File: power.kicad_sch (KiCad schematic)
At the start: 25 parts, among them IC4 BQ27441DRZR-G1A, IC5 MCP73811T-420I_OT, IC6 TPS62237DRYR, IC7 ST1S15J18R, U1 TPS62233DRYR

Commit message: Add company name (using github URL), date, and change revision number to all schematic pages
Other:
- company: (none) -> github.com/fuad1502/open-running-watch-hw
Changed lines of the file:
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@@
 	(title_block
 		(title "Open Running Watch")
-		(rev "A")
+		(date "2024-04-12")
+		(rev "0.1.0")
+		(company "github.com/fuad1502/open-running-watch-hw")
 	)
 	(junction

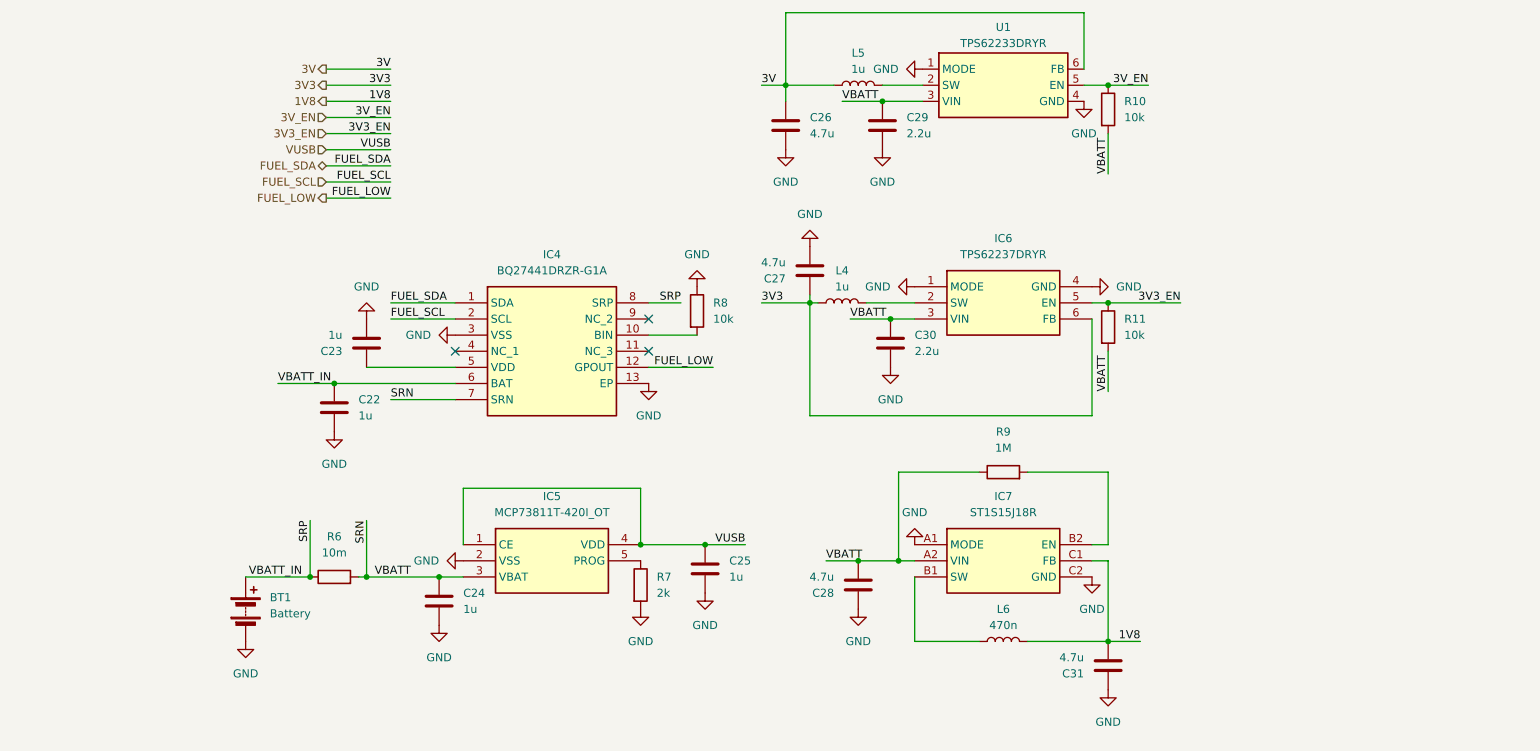
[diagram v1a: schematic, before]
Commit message: Add 5V boost switching regulator
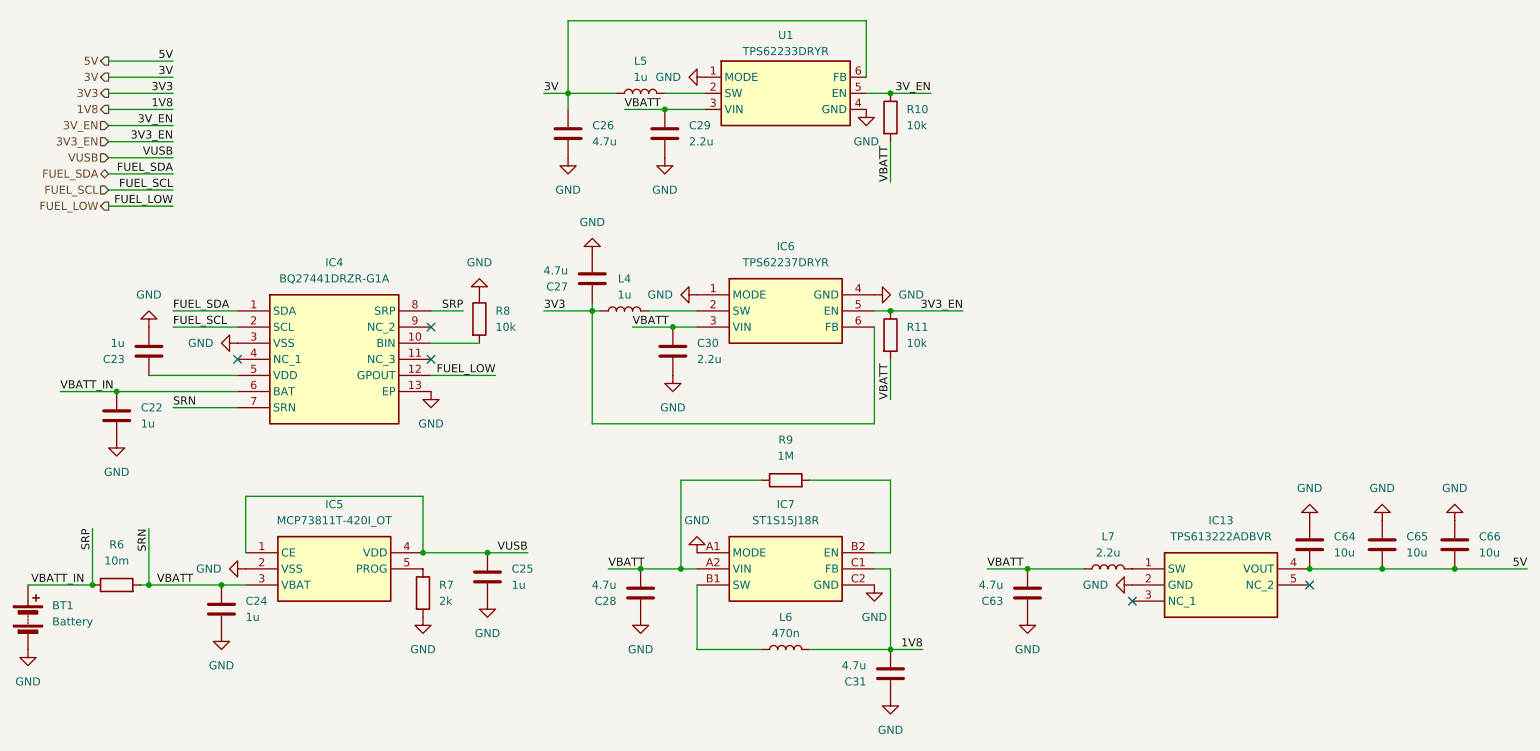
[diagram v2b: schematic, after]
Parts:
- added C63: 4.7u, Capacitor_SMD:C_0402_1005Metric_Pad0.74x0.62mm_HandSolder, symbol Device:C
- added C64, C65, C66: 10u, Capacitor_SMD:C_0603_1608Metric, symbol Device:C
- added IC13: TPS613222ADBVR, SOT95P280X145-5N, symbol TPS613222ADBVR:TPS613222ADBVR
- added L7: 2.2u, Inductor_SMD:L_1008_2520Metric, symbol Device:L
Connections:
- net GND: now also C63.1, C64.1, C65.1, C66.1, IC13.2 (GND)
- net SRN: now also C63.2, L7.1
- new net: IC13.1 (SW), L7.2
- new net 5V: C64.2, C65.2, C66.2, IC13.4 (VOUT)
- no-connect marks 3 -> 5
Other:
- moved on the sheet: BT1, C22, C23, C24, C25, C26, C27, C28, C29, C30, C31, IC4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

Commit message: Changed to smaller tactile switch
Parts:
- IC13: footprint SOT95P280X145-5N -> TPS613222ADBVR:SOT95P280X145-5N
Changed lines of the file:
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@@
 			)
 		)
-		(property "Footprint" "SOT95P280X145-5N"
+		(property "Footprint" "TPS613222ADBVR:SOT95P280X145-5N"
 			(at 233.68 221.92 0)
 			(effects

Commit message: Changed hand soldered footprints to normal footprints
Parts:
- C22, C23, C24, C25: footprint Capacitor_SMD:C_0603_1608Metric_Pad1.08x0.95mm_HandSolder -> Capacitor_SMD:C_0603_1608Metric
- C26, C27, C28, C29, C30, C31, C63: footprint Capacitor_SMD:C_0402_1005Metric_Pad0.74x0.62mm_HandSolder -> Capacitor_SMD:C_0402_1005Metric
- L4, L5: footprint Inductor_SMD:L_1008_2520Metric_Pad1.43x2.20mm_HandSolder -> Inductor_SMD:L_1008_2520Metric
- L6: footprint Inductor_SMD:L_0805_2012Metric_Pad1.05x1.20mm_HandSolder -> Inductor_SMD:L_0805_2012Metric
- R10, R11, R7, R8, R9: footprint Resistor_SMD:R_0402_1005Metric_Pad0.72x0.64mm_HandSolder -> Resistor_SMD:R_0402_1005Metric
- R6: footprint Resistor_SMD:R_1206_3216Metric_Pad1.30x1.75mm_HandSolder -> Resistor_SMD:R_1206_3216Metric
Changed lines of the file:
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@@
 			)
 		)
-		(property "Footprint" "Resistor_SMD:R_0402_1005Metric_Pad0.72x0.64mm_HandSolder"
+		(property "Footprint" "Resistor_SMD:R_0402_1005Metric"
 			(at 169.672 55.88 90)
 			(effects
@@
 			)
 		)
-		(property "Footprint" "Resistor_SMD:R_0402_1005Metric_Pad0.72x0.64mm_HandSolder"
+		(property "Footprint" "Resistor_SMD:R_0402_1005Metric"
 			(at 154.94 114.808 90)
 			(effects
@@
 			)
 		)
-		(property "Footprint" "Inductor_SMD:L_1008_2520Metric_Pad1.43x2.20mm_HandSolder"
+		(property "Footprint" "Inductor_SMD:L_1008_2520Metric"
 			(at 129.54 86.36 0)
 			(effects
@@
 			)
 		)
-		(property "Footprint" "Capacitor_SMD:C_0603_1608Metric_Pad1.08x0.95mm_HandSolder"
+		(property "Footprint" "Capacitor_SMD:C_0603_1608Metric"
 			(at 53.6448 88.9 0)
 			(effects
@@
 			)
 		)
-		(property "Footprint" "Capacitor_SMD:C_0603_1608Metric_Pad1.08x0.95mm_HandSolder"
+		(property "Footprint" "Capacitor_SMD:C_0603_1608Metric"
 			(at 108.9152 132.08 0)
 			(effects
@@
 			)
 		)
-		(property "Footprint" "Capacitor_SMD:C_0603_1608Metric_Pad1.08x0.95mm_HandSolder"
+		(property "Footprint" "Capacitor_SMD:C_0603_1608Metric"
 			(at 50.4952 106.68 0)
 			(effects
@@
 			)
 		)
-		(property "Footprint" "Capacitor_SMD:C_0402_1005Metric_Pad0.74x0.62mm_HandSolder"
+		(property "Footprint" "Capacitor_SMD:C_0402_1005Metric"
 			(at 123.4948 77.47 0)
 			(effects
@@
 			)
 		)
-		(property "Footprint" "Inductor_SMD:L_1008_2520Metric_Pad1.43x2.20mm_HandSolder"
+		(property "Footprint" "Inductor_SMD:L_1008_2520Metric"
 			(at 132.08 52.07 0)
 			(effects
@@
 			)
 		)
-		(property "Footprint" "Resistor_SMD:R_0402_1005Metric_Pad0.72x0.64mm_HandSolder"
+		(property "Footprint" "Resistor_SMD:R_0402_1005Metric"
 			(at 96.012 130.81 90)
 			(effects
@@
 			)
 		)
-		(property "Footprint" "Capacitor_SMD:C_0402_1005Metric_Pad0.74x0.62mm_HandSolder"
+		(property "Footprint" "Capacitor_SMD:C_0402_1005Metric"
 			(at 121.6152 62.23 0)
 			(effects
@@
 			)
 		)
-		(property "Footprint" "Capacitor_SMD:C_0402_1005Metric_Pad0.74x0.62mm_HandSolder"
+		(property "Footprint" "Capacitor_SMD:C_0402_1005Metric"
 			(at 138.1252 96.52 0)
 			(effects
@@
 			)
 		)
-		(property "Footprint" "Capacitor_SMD:C_0402_1005Metric_Pad0.74x0.62mm_HandSolder"
+		(property "Footprint" "Capacitor_SMD:C_0402_1005Metric"
 			(at 131.1148 127 0)
 			(effects
@@
 			)
 		)
-		(property "Footprint" "Capacitor_SMD:C_0603_1608Metric_Pad1.08x0.95mm_HandSolder"
+		(property "Footprint" "Capacitor_SMD:C_0603_1608Metric"
 			(at 67.0052 137.16 0)
 			(effects
@@
 			)
 		)
-		(property "Footprint" "Capacitor_SMD:C_0402_1005Metric_Pad0.74x0.62mm_HandSolder"
+		(property "Footprint" "Capacitor_SMD:C_0402_1005Metric"
 			(at 170.4848 139.7 0)
 			(effects
@@
 			)
 		)
-		(property "Footprint" "Inductor_SMD:L_0805_2012Metric_Pad1.05x1.20mm_HandSolder"
+		(property "Footprint" "Inductor_SMD:L_0805_2012Metric"
 			(at 154.94 139.7 0)
 			(effects
@@
 			)
 		)
-		(property "Footprint" "Resistor_SMD:R_1206_3216Metric_Pad1.30x1.75mm_HandSolder"
+		(property "Footprint" "Resistor_SMD:R_1206_3216Metric"
 			(at 49.53 131.318 90)
 			(effects
@@
 			)
 		)
-		(property "Footprint" "Capacitor_SMD:C_0402_1005Metric_Pad0.74x0.62mm_HandSolder"
+		(property "Footprint" "Capacitor_SMD:C_0402_1005Metric"
 			(at 192.0748 127 0)
 			(effects
@@
 			)
 		)
-		(property "Footprint" "Resistor_SMD:R_0402_1005Metric_Pad0.72x0.64mm_HandSolder"
+		(property "Footprint" "Resistor_SMD:R_0402_1005Metric"
 			(at 104.902 87.63 90)
 			(effects
@@
 			)
 		)
-		(property "Footprint" "Capacitor_SMD:C_0402_1005Metric_Pad0.74x0.62mm_HandSolder"
+		(property "Footprint" "Capacitor_SMD:C_0402_1005Metric"
 			(at 136.8552 62.23 0)
 			(effects
@@
 			)
 		)
-		(property "Footprint" "Resistor_SMD:R_0402_1005Metric_Pad0.72x0.64mm_HandSolder"
+		(property "Footprint" "Resistor_SMD:R_0402_1005Metric"
 			(at 169.672 90.17 90)
 			(effects
